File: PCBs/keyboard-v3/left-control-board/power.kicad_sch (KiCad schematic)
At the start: 10 parts, among them U701 TPS62290TDRVRQ1

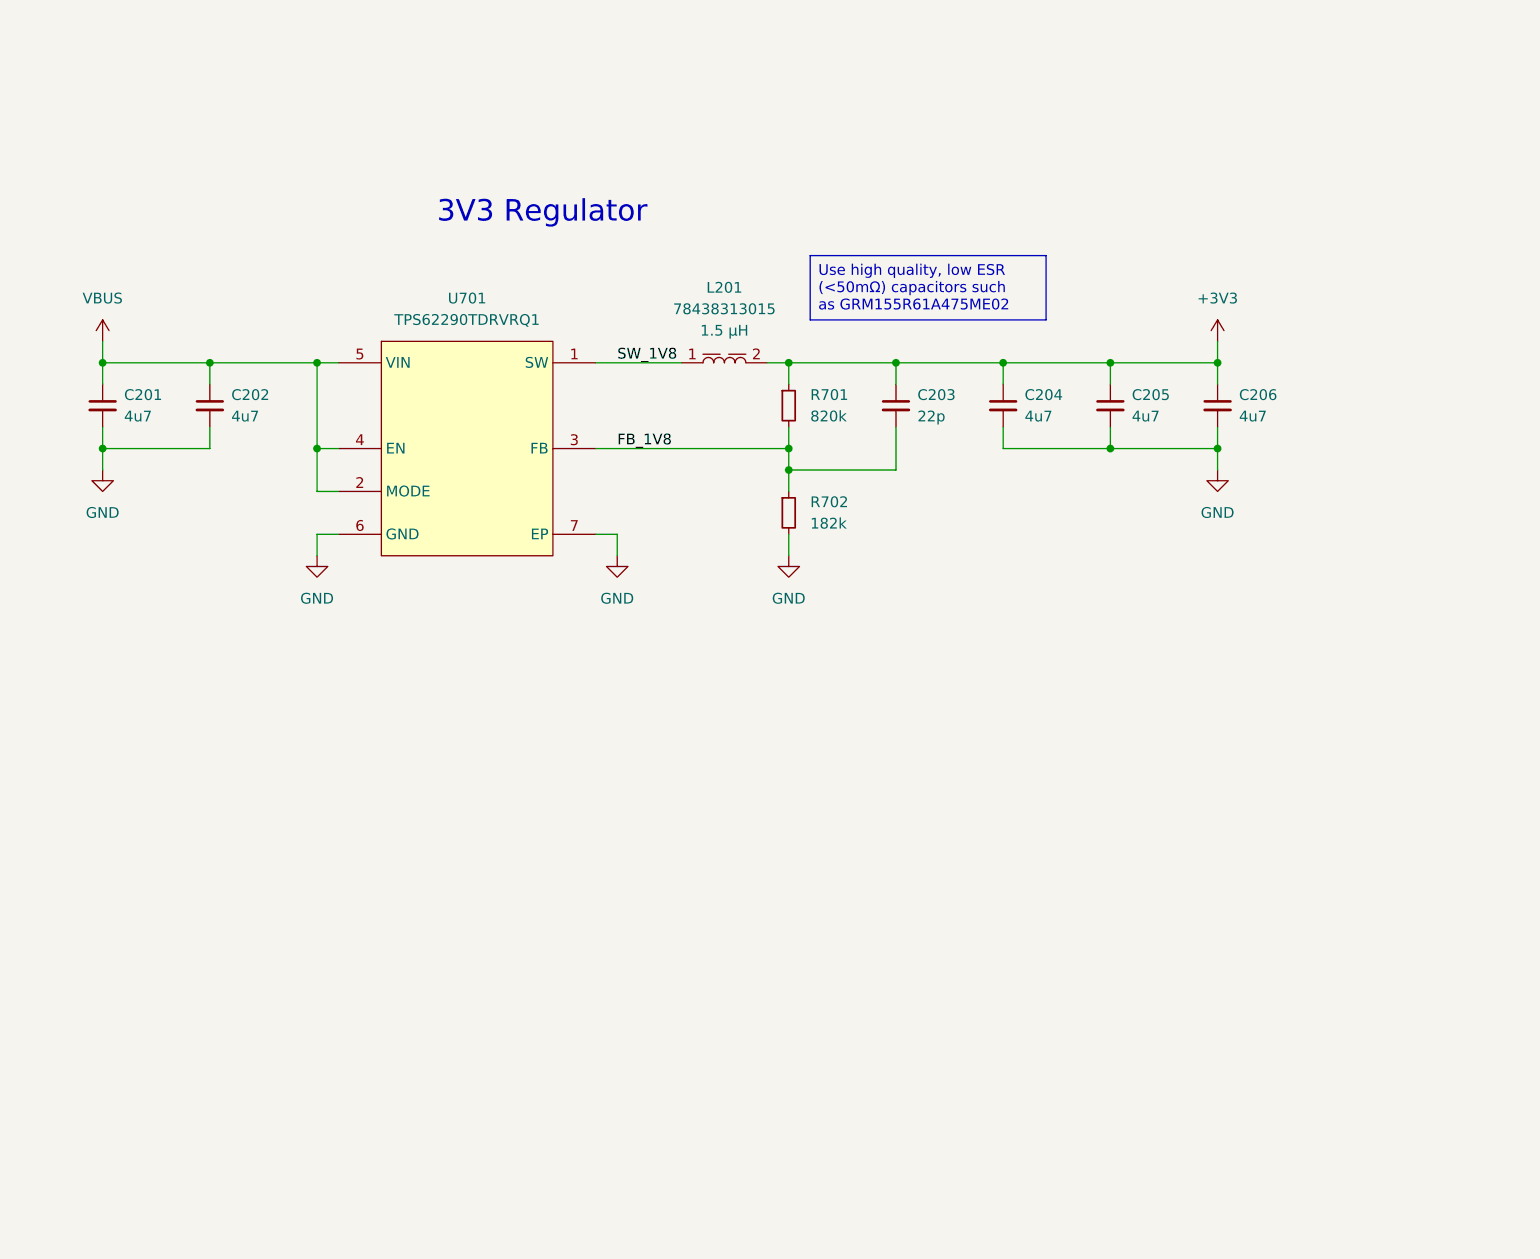
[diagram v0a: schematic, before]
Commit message: Left knob board done
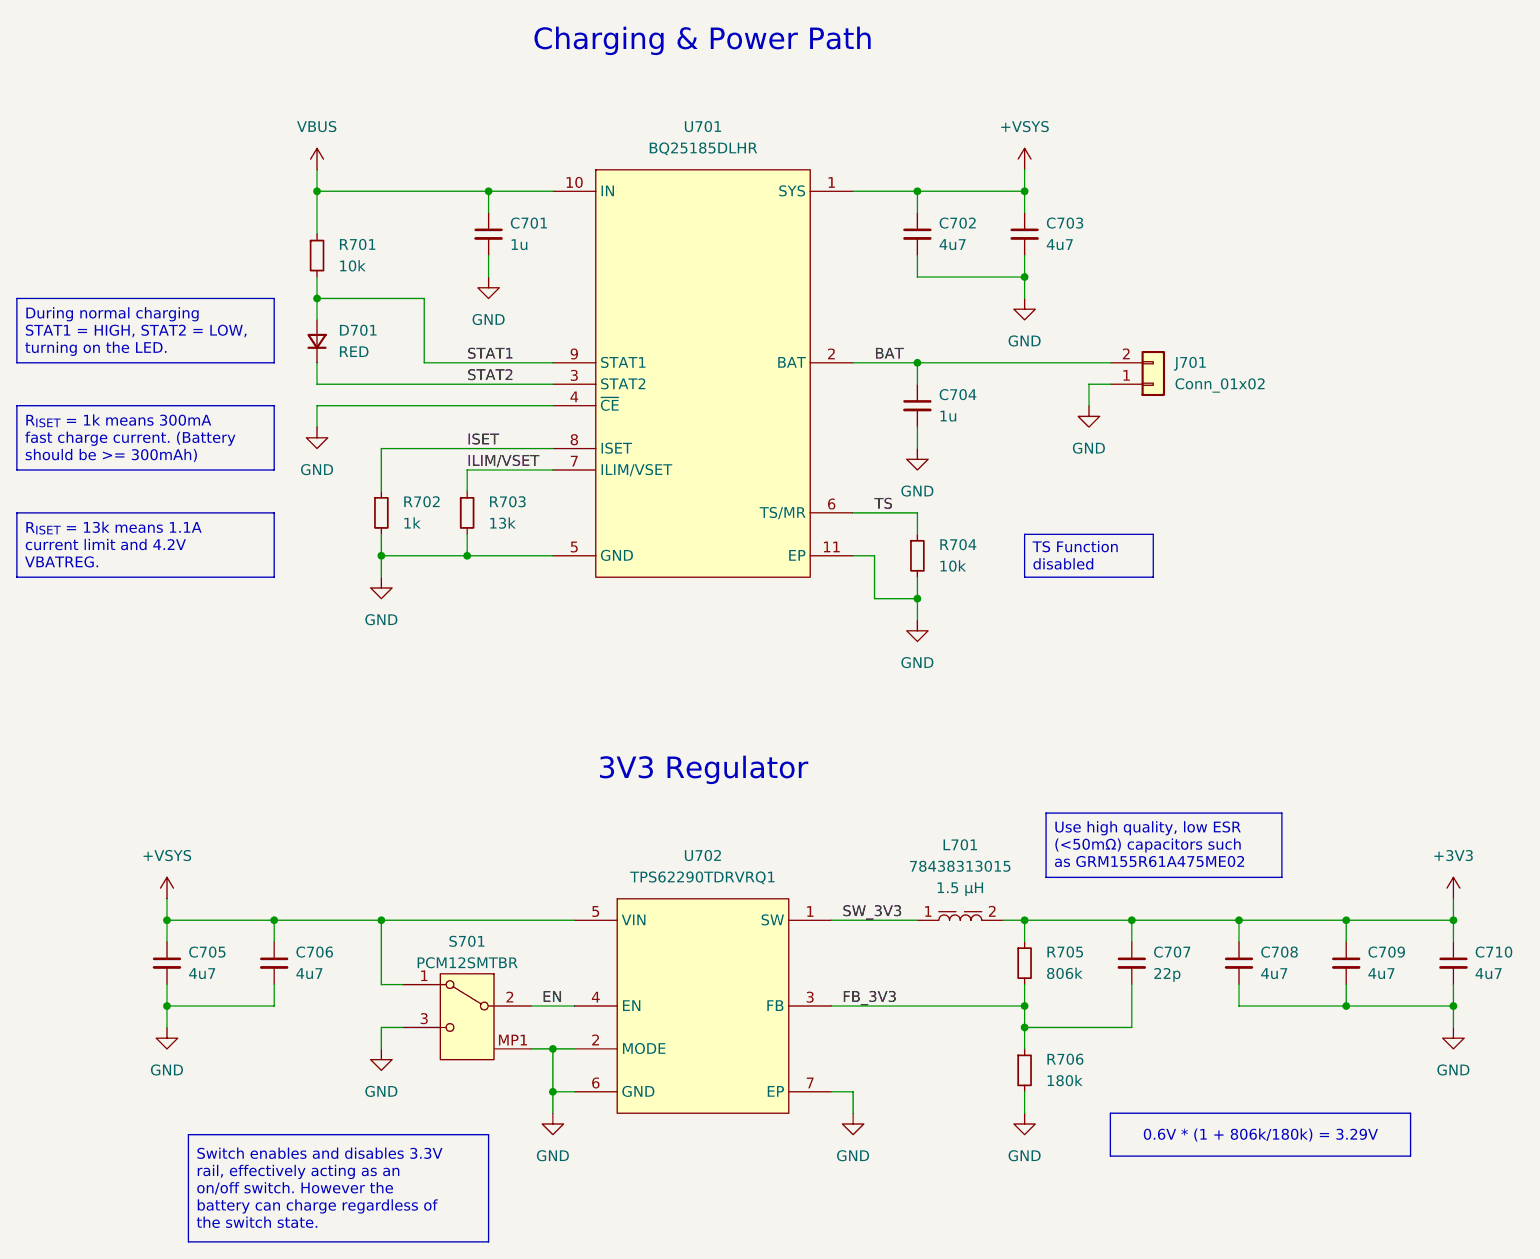
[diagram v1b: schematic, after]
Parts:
- added C701, C704: 1u, project_footprints:C_0402, symbol DEV:C_SMALL
- added C702, C703: 4u7, project_footprints:C_0402, symbol DEV:C_SMALL
- added D701: RED, project_footprints:LED_0402, symbol Device:D_Small
- added J701: Conn_01x02, Connector_JST:JST_PH_S2B-PH-K_1x02_P2.00mm_Horizontal, symbol Connector_Generic:Conn_01x02
- added R701, R704: 10k, project_footprints:R_0402, symbol DEV:R_SMALL
- added R702: 1k, project_footprints:R_0402, symbol DEV:R_SMALL
- added R703: 13k, project_footprints:R_0402, symbol DEV:R_SMALL
- added S701: PCM12SMTBR, project_footprints:PCM12SMTBR, symbol MECH:PCM12SMTBR
- added U701: BQ25185DLHR, project_footprints:SON40P220X200X80-11N, symbol CHARGING:BQ25185DLHR
- R705: renamed from R701; value 820k -> 806k
- R706: renamed from R702; value 182k -> 180k
- renumbered C201 to C705, C202 to C706, C203 to C707, C204 to C708, C205 to C709, C206 to C710, L201 to L701, U701 to U702
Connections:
- net GND: now also U702.2 (MODE), C701.2, C702.2, C703.2, C704.2, J701.1 (Pin_1), R702.2, R703.2, R704.2, S701.3 (NO), S701.MP1, S701.MP2, S701.MP3, S701.MP4, U701.11 (EP), U701.4 (~{CE}), U701.5 (GND)
- net VBUS: now also C701.1, R701.1, U701.10 (IN); no longer C705.1, C706.1, U702.2 (MODE), U702.4 (EN), U702.5 (VIN)
- net FB_1V8 renamed FB_3V3
- net SW_1V8 renamed SW_3V3
- new net +VSYS: C702.1, C703.1, C705.1, C706.1, S701.1 (NC), U701.1 (SYS), U702.5 (VIN)
- new net BAT: C704.1, J701.2 (Pin_2), U701.2 (BAT)
- new net EN: S701.2 (COM), U702.4 (EN)
- new net ILIM/VSET: R703.1, U701.7 (ILIM/VSET)
- new net ISET: R702.1, U701.8 (ISET)
- new net STAT1: D701.2 (A), R701.2, U701.9 (STAT1)
- new net STAT2: D701.1 (K), U701.3 (STAT2)
- new net TS: R704.1, U701.6 (TS/MR)
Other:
- note added: "Charging & Power Path"
- moved on the sheet: C705, C706, C707, C708, C709, C710, L701, R705, R706, U702

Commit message: Keyboard v3 hardware done
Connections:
- net +VSYS: now also S701.3 (NO); no longer S701.1 (NC)
- net GND: now also S701.1 (NC); no longer S701.3 (NO)

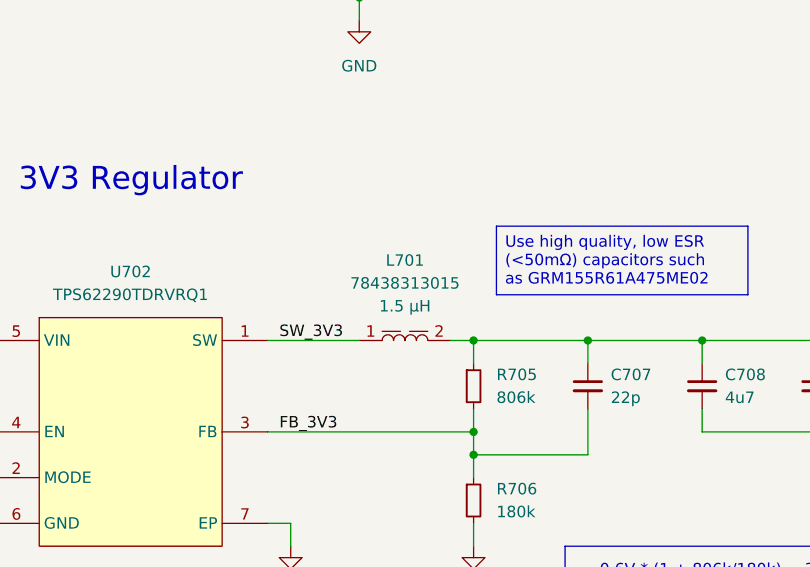
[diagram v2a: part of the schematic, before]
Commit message: Added v3 left BOMs and updated buck inductor
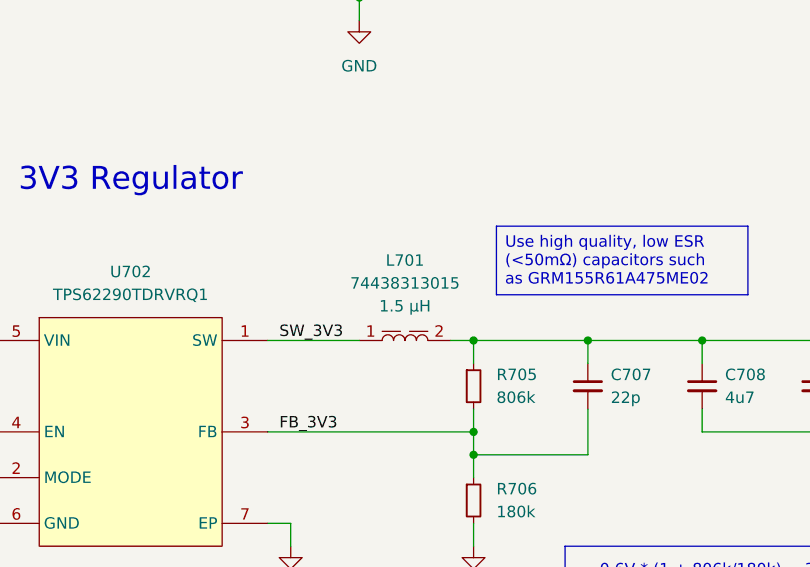
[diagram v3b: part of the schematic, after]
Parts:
- L701: value 78438313015 -> 74438313015; footprint project_footprints:L_Wurth_WE-MAIA-1610 -> project_footprints:L_Wurth_WE-MAPI-1610; symbol PWR-IND:1610_78438313015 -> PWR-IND:74438313015; Match Code WE-MAIA -> WE-MAPI; Part Number 78438313015 -> 74438313015; Published Date 20250429 -> 20250320; RDC typ. (mΩ) (none) -> 189.0; VOP (V) (none) -> 80
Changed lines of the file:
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@@
 	)
 	(symbol
-		(lib_id "PWR-IND:1610_78438313015")
+		(lib_id "PWR-IND:74438313015")
 		(at 182.88 129.54 0)
 		(unit 1)
@@
 			)
 		)
-		(property "Value" "78438313015"
+		(property "Value" "74438313015"
 			(at 182.88 123.19 0)
 			(effects
@@
 			)
 		)
-		(property "Footprint" "project_footprints:L_Wurth_WE-MAIA-1610"
-			(at 195.58 109.22 0)
+		(property "Footprint" "project_footprints:L_Wurth_WE-MAPI-1610"
+			(at 182.88 121.92 0)
 			(effects
 				(font
 					(size 1.27 1.27)
 				)
-				(justify left)
 				(hide yes)
 			)
 		)
-		(property "Datasheet" "https://www.we-online.com/catalog/datasheet/78438313015.pdf?ki"
-			(at 195.58 111.76 0)
+		(property "Datasheet" "https://www.we-online.com/catalog/datasheet/74438313015.pdf?ki"
+			(at 234.95 111.76 0)
 			(effects
 				(font
 					(size 1.27 1.27)
 				)
-				(justify left)
 				(hide yes)
 			)
 		)
-		(property "Description" "Single Coil Power Inductor"
+		(property "Description" "Shielded Power Inductor"
 			(at 182.88 129.54 0)
 			(effects
@@
 		)
 		(property "Manufacturer" "Wurth Elektronik"
-			(at 195.58 114.3 0)
+			(at 234.95 114.3 0)
 			(effects
 				(font
 					(size 1.27 1.27)
 				)
-				(justify left)
 				(hide yes)
 			)
 		)
 		(property "Manufacturer URL" "https://www.we-online.com"
-			(at 195.58 116.84 0)
+			(at 234.95 116.84 0)
 			(effects
 				(font
 					(size 1.27 1.27)
 				)
-				(justify left)
 				(hide yes)
 			)
 		)
-		(property "Published Date" "20250429"
-			(at 195.58 119.38 0)
+		(property "Published Date" "20250320"
+			(at 234.95 119.38 0)
 			(effects
 				(font
 					(size 1.27 1.27)
 				)
-				(justify left)
 				(hide yes)
 			)
 		)
-		(property "Match Code" "WE-MAIA"
-			(at 195.58 121.92 0)
+		(property "Match Code" "WE-MAPI"
+			(at 234.95 121.92 0)
 			(effects
 				(font
 					(size 1.27 1.27)
 				)
-				(justify left)
 				(hide yes)
 			)
 		)
-		(property "Part Number" "78438313015"
-			(at 195.58 124.46 0)
+		(property "Part Number" "74438313015"
+			(at 234.95 124.46 0)
 			(effects
 				(font
 					(size 1.27 1.27)
 				)
-				(justify left)
 				(hide yes)
 			)
 		)
 		(property "Size" "1610"
-			(at 195.58 127 0)
+			(at 234.95 127 0)
 			(effects
 				(font
 					(size 1.27 1.27)
 				)
-				(justify left)
 				(hide yes)
 			)
 		)
 		(property "Mounting Technology" "SMT"
-			(at 195.58 129.54 0)
+			(at 234.95 129.54 0)
 			(effects
 				(font
 					(size 1.27 1.27)
 				)
-				(justify left)
 				(hide yes)
 			)
 		)
 		(property "L (µH)" "1.5"
-			(at 195.58 132.08 0)
+			(at 234.95 132.08 0)
 			(effects
 				(font
 					(size 1.27 1.27)
 				)
-				(justify left)
 				(hide yes)
 			)
@@
 		)
 		(property "ISAT,30% (A)" "3.45"
-			(at 195.58 137.16 0)
+			(at 234.95 137.16 0)
 			(effects
 				(font
 					(size 1.27 1.27)
 				)
-				(justify left)
 				(hide yes)
 			)
@@
 		)
 		(property "fres (MHz)" "90.0"
-			(at 195.58 142.24 0)
+			(at 234.95 142.24 0)
 			(effects
 				(font
 					(size 1.27 1.27)
 				)
-				(justify left)
 				(hide yes)
 			)
 		)
 		(property "IRP,40K (A)" "1.8"
-			(at 195.58 144.78 0)
+			(at 234.95 134.62 0)
 			(effects
 				(font
 					(size 1.27 1.27)
 				)
-				(justify left)
 				(hide yes)
 			)
@@
 			)
 		)
+		(property "RDC typ. (mΩ)" "189.0"
+			(at 234.95 139.7 0)
+			(effects
+				(font
+					(size 1.27 1.27)
+				)
+				(hide yes)
+			)
+		)
+		(property "VOP (V)" "80"
+			(at 234.95 144.78 0)
+			(effects
+				(font
+					(size 1.27 1.27)
+				)
+				(hide yes)
+			)
+		)
